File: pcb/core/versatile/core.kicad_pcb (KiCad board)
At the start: 2 copper layers, 79.3 x 78.9 mm, 33 parts, among them J1 Conn_01x11, J2 Conn_01x11, J3 Conn_01x04, SW1 SW_Push_45deg, SW10 RotaryEncoder_Switch, SW11 RotaryEncoder_Switch, SW12 RotaryEncoder_Switch, SW13 RotaryEncoder_Switch, SW2 SW_Push_45deg, SW3 SW_Push_45deg, SW4 SW_Push_45deg, SW5 SW_Push_45deg, SW6 SW_Push_45deg, SW7 SW_Push_45deg, SW8 SW_Push_45deg, SW9 SW_Push_45deg, U1 Helios

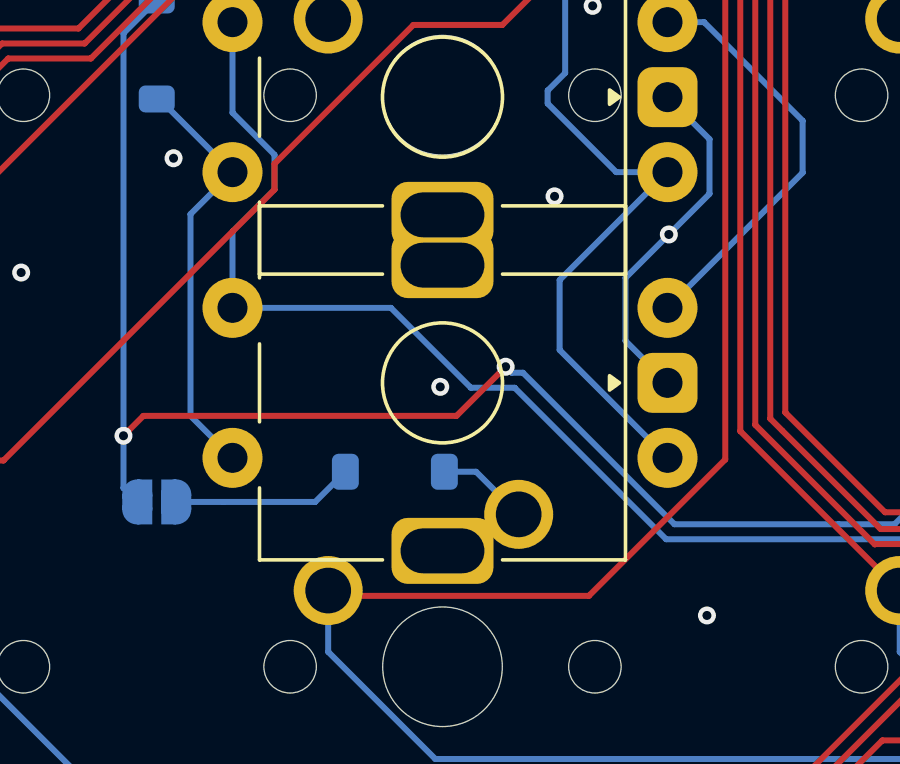
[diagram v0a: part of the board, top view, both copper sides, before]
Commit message: renamed core pcbs
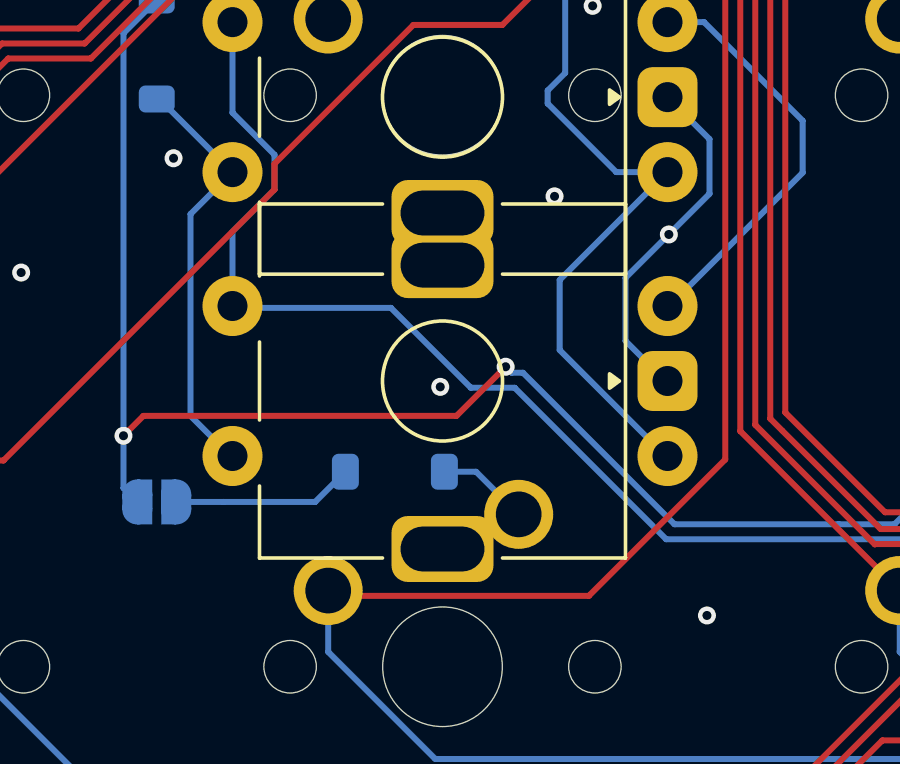
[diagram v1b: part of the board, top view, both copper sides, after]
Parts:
- moved SW10 0.06 mm to (198.2, 191.6)

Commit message: added versions
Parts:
- added REF**: OSHW-Symbol_6.7x6mm_Copper, Symbol:OSHW-Symbol_6.7x6mm_Copper, F.Cu at (225.1, 206.2)
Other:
- board text added: "floookay.de/barnacle versatile core v1.1 CERN-OHL-S"
